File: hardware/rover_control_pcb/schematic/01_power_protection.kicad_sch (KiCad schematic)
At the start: 0 parts

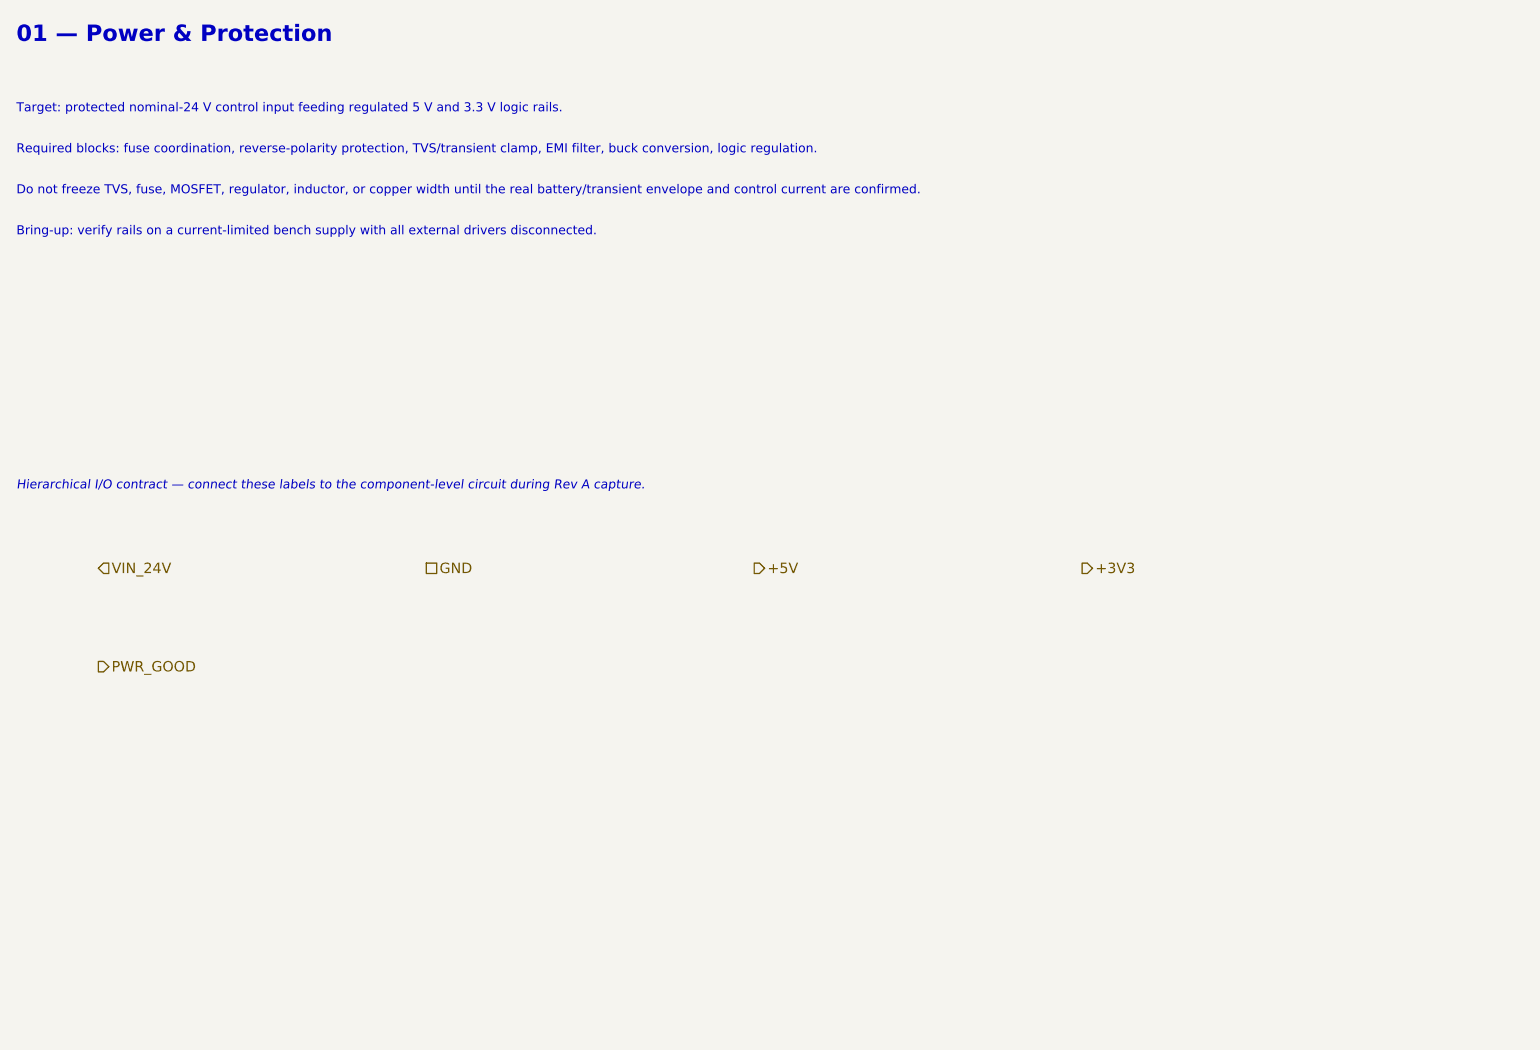
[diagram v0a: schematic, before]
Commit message: Implement Rev A power-stage candidate circuit
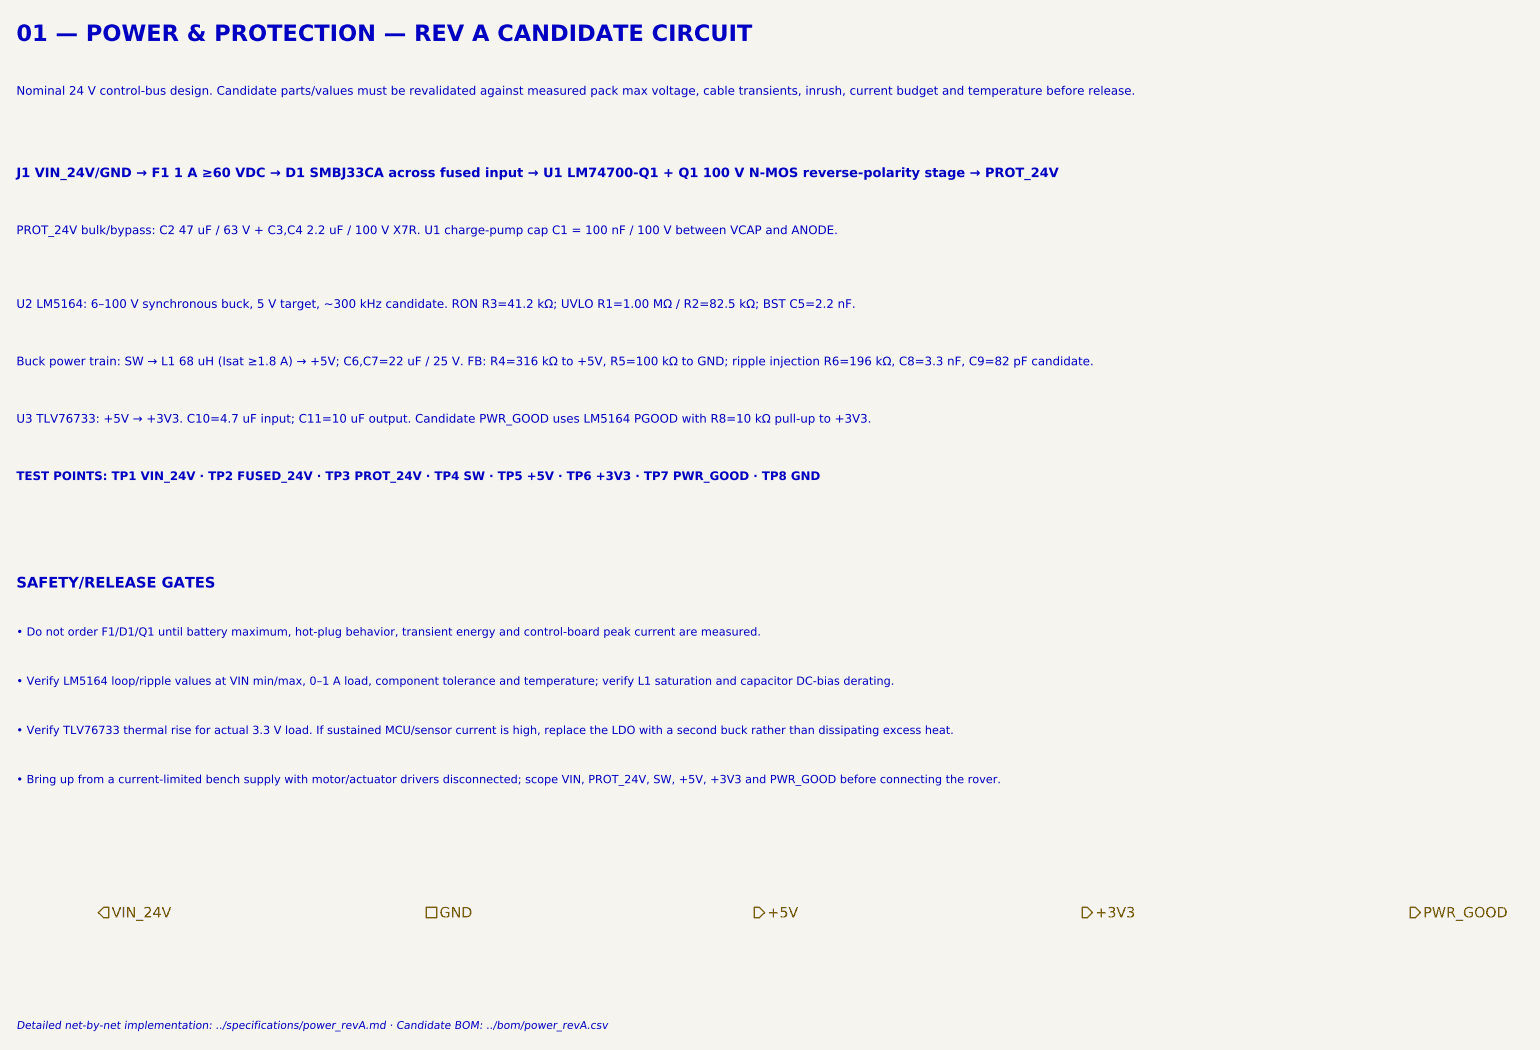
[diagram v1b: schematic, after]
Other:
- note added: "01 — POWER & PROTECTION — REV A CANDIDATE CIRCUIT"
- note added: "Buck power train: SW → L1 68 uH (Isat ≥1.8 A) → +5V; C6,C7=22 uF / 25 V. FB: R4=316 kΩ to +5V, R5=100 kΩ to GND; ripple injection R6=196 kΩ, C8=3.3 nF, C9=82 pF candidate."
- note added: "Detailed net-by-net implementation: ../specifications/power_revA.md · Candidate BOM: ../bom/power_revA.csv"
- note added: "J1 VIN_24V/GND → F1 1 A ≥60 VDC → D1 SMBJ33CA across fused input → U1 LM74700-Q1 + Q1 100 V N-MOS reverse-polarity stage → PROT_24V"
- note added: "Nominal 24 V control-bus design. Candidate parts/values must be revalidated against measured pack max voltage, cable transients, inrush, current budget and temperature before release."
- note added: "PROT_24V bulk/bypass: C2 47 uF / 63 V + C3,C4 2.2 uF / 100 V X7R. U1 charge-pump cap C1 = 100 nF / 100 V between VCAP and ANODE."
- note added: "SAFETY/RELEASE GATES"
- note added: "TEST POINTS: TP1 VIN_24V · TP2 FUSED_24V · TP3 PROT_24V · TP4 SW · TP5 +5V · TP6 +3V3 · TP7 PWR_GOOD · TP8 GND"
- note added: "U2 LM5164: 6–100 V synchronous buck, 5 V target, ~300 kHz candidate. RON R3=41.2 kΩ; UVLO R1=1.00 MΩ / R2=82.5 kΩ; BST C5=2.2 nF."
- note added: "U3 TLV76733: +5V → +3V3. C10=4.7 uF input; C11=10 uF output. Candidate PWR_GOOD uses LM5164 PGOOD with R8=10 kΩ pull-up to +3V3."
- note added: "• Bring up from a current-limited bench supply with motor/actuator drivers disconnected; scope VIN, PROT_24V, SW, +5V, +3V3 and PWR_GOOD before connecting the rover."
- note added: "• Do not order F1/D1/Q1 until battery maximum, hot-plug behavior, transient energy and control-board peak current are measured."
- note added: "• Verify LM5164 loop/ripple values at VIN min/max, 0–1 A load, component tolerance and temperature; verify L1 saturation and capacitor DC-bias derating."
- note added: "• Verify TLV76733 thermal rise for actual 3.3 V load. If sustained MCU/sensor current is high, replace the LDO with a second buck rather than dissipating excess heat."
- note removed: "01 — Power & Protection"
- note removed: "Bring-up: verify rails on a current-limited bench supply with all external drivers disconnected."
- note removed: "Do not freeze TVS, fuse, MOSFET, regulator, inductor, or copper width until the real battery/transient envelope and control current are confirmed."
- note removed: "Hierarchical I/O contract — connect these labels to the component-level circuit during Rev A capture."
- note removed: "Required blocks: fuse coordination, reverse-polarity protection, TVS/transient clamp, EMI filter, buck conversion, logic regulation."
- note removed: "Target: protected nominal-24 V control input feeding regulated 5 V and 3.3 V logic rails."
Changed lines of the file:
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@@
     (title "01 — Power & Protection")
     (date "2026-09-13")
-    (rev "Rev A architecture")
+    (rev "Rev A candidate circuit")
     (company "UHCL Lunar Hawks")
-    (comment 1 "Interface scaffold; component selection/ERC pending design inputs.")
+    (comment 1 "Candidate component topology captured; ERC/layout/fabrication validation pending.")
+    (comment 2 "High-current motor/actuator power remains off this PCB.")
   )
-  (text "01 — Power & Protection" (exclude_from_sim no) (at 20 15 0) (effects (font (size 2 2) (bold yes)) (justify left)))
-  (text "Target: protected nominal-24 V control input feeding regulated 5 V and 3.3 V logic rails." (exclude_from_sim no) (at 20 24 0) (effects (font (size 1.1 1.1)) (justify left)))
-  (text "Required blocks: fuse coordination, reverse-polarity protection, TVS/transient clamp, EMI filter, buck conversion, logic regulation." (exclude_from_sim no) (at 20 29 0) (effects (font (size 1.1 1.1)) (justify left)))
-  (text "Do not freeze TVS, fuse, MOSFET, regulator, inductor, or copper width until the real battery/transient envelope and control current are confirmed." (exclude_from_sim no) (at 20 34 0) (effects (font (size 1.1 1.1)) (justify left)))
-  (text "Bring-up: verify rails on a current-limited bench supply with all external drivers disconnected." (exclude_from_sim no) (at 20 39 0) (effects (font (size 1.1 1.1)) (justify left)))
-  (text "Hierarchical I/O contract — connect these labels to the component-level circuit during Rev A capture." (exclude_from_sim no) (at 20 70 0) (effects (font (size 1.1 1.1) (italic yes)) (justify left)))
-  (hierarchical_label "VIN_24V" (shape input) (at 30 80 0) (effects (font (size 1.27 1.27)) (justify left)))
-  (hierarchical_label "GND" (shape passive) (at 70 80 0) (effects (font (size 1.27 1.27)) (justify left)))
-  (hierarchical_label "+5V" (shape output) (at 110 80 180) (effects (font (size 1.27 1.27)) (justify left)))
-  (hierarchical_label "+3V3" (shape output) (at 150 80 180) (effects (font (size 1.27 1.27)) (justify left)))
-  (hierarchical_label "PWR_GOOD" (shape output) (at 30 92 180) (effects (font (size 1.27 1.27)) (justify left)))
+  (text "01 — POWER & PROTECTION — REV A CANDIDATE CIRCUIT" (exclude_from_sim no) (at 20 15 0)
+    (effects (font (size 2 2) (bold yes)) (justify left))
+)
+  (text "Nominal 24 V control-bus design. Candidate parts/values must be revalidated against measured pack max voltage, cable transients, inrush, current budget and temperature before release." (exclude_from_sim no) (at 20 22 0)
+    (effects (font (size 1.05 1.05)) (justify left))
+)
+  (text "J1 VIN_24V/GND → F1 1 A ≥60 VDC → D1 SMBJ33CA across fused input → U1 LM74700-Q1 + Q1 100 V N-MOS reverse-polarity stage → PROT_24V" (exclude_from_sim no) (at 20 32 0)
+    (effects (font (size 1.15 1.15) (bold yes)) (justify left))
+)
+  (text "PROT_24V bulk/bypass: C2 47 uF / 63 V + C3,C4 2.2 uF / 100 V X7R. U1 charge-pump cap C1 = 100 nF / 100 V between VCAP and ANODE." (exclude_from_sim no) (at 20 39 0)
+    (effects (font (size 1.05 1.05)) (justify left))
+)
+  (text "U2 LM5164: 6–100 V synchronous buck, 5 V target, ~300 kHz candidate. RON R3=41.2 kΩ; UVLO R1=1.00 MΩ / R2=82.5 kΩ; BST C5=2.2 nF." (exclude_from_sim no) (at 20 48 0)
+    (effects (font (size 1.05 1.05)) (justify left))
+)
+  (text "Buck power train: SW → L1 68 uH (Isat ≥1.8 A) → +5V; C6,C7=22 uF / 25 V. FB: R4=316 kΩ to +5V, R5=100 kΩ to GND; ripple injection R6=196 kΩ, C8=3.3 nF, C9=82 pF candidate." (exclude_from_sim no) (at 20 55 0)
+    (effects (font (size 1.05 1.05)) (justify left))
+)
+  (text "U3 TLV76733: +5V → +3V3. C10=4.7 uF input; C11=10 uF output. Candidate PWR_GOOD uses LM5164 PGOOD with R8=10 kΩ pull-up to +3V3." (exclude_from_sim no) (at 20 62 0)
+    (effects (font (size 1.05 1.05)) (justify left))
+)
+  (text "TEST POINTS: TP1 VIN_24V · TP2 FUSED_24V · TP3 PROT_24V · TP4 SW · TP5 +5V · TP6 +3V3 · TP7 PWR_GOOD · TP8 GND" (exclude_from_sim no) (at 20 69 0)
+    (effects (font (size 1.05 1.05) (bold yes)) (justify left))
+)
+  (text "SAFETY/RELEASE GATES" (exclude_from_sim no) (at 20 82 0)
+    (effects (font (size 1.3 1.3) (bold yes)) (justify left))
+)
+  (text "• Do not order F1/D1/Q1 until battery maximum, hot-plug behavior, transient energy and control-board peak current are measured." (exclude_from_sim no) (at 20 88 0)
+    (effects (font (size 1 1)) (justify left))
+)
+  (text "• Verify LM5164 loop/ripple values at VIN min/max, 0–1 A load, component tolerance and temperature; verify L1 saturation and capacitor DC-bias derating." (exclude_from_sim no) (at 20 94 0)
+    (effects (font (size 1 1)) (justify left))
+)
+  (text "• Verify TLV76733 thermal rise for actual 3.3 V load. If sustained MCU/sensor current is high, replace the LDO with a second buck rather than dissipating excess heat." (exclude_from_sim no) (at 20 100 0)
+    (effects (font (size 1 1)) (justify left))
+)
+  (text "• Bring up from a current-limited bench supply with motor/actuator drivers disconnected; scope VIN, PROT_24V, SW, +5V, +3V3 and PWR_GOOD before connecting the rover." (exclude_from_sim no) (at 20 106 0)
+    (effects (font (size 1 1)) (justify left))
+)
+  (hierarchical_label "VIN_24V" (shape input) (at 30 122 0)
+    (effects (font (size 1.27 1.27)) (justify left))
+)
+  (hierarchical_label "GND" (shape passive) (at 70 122 0)
+    (effects (font (size 1.27 1.27)) (justify left))
+)
+  (hierarchical_label "+5V" (shape output) (at 110 122 180)
+    (effects (font (size 1.27 1.27)) (justify left))
+)
+  (hierarchical_label "+3V3" (shape output) (at 150 122 180)
+    (effects (font (size 1.27 1.27)) (justify left))
+)
+  (hierarchical_label "PWR_GOOD" (shape output) (at 190 122 180)
+    (effects (font (size 1.27 1.27)) (justify left))
+)
+  (text "Detailed net-by-net implementation: ../specifications/power_revA.md · Candidate BOM: ../bom/power_revA.csv" (exclude_from_sim no) (at 20 136 0)
+    (effects (font (size 0.95 0.95) (italic yes)) (justify left))
+)
   (sheet_instances (path "/" (page "2")))
   (embedded_fonts no)
